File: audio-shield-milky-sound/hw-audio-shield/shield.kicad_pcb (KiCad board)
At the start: 2 copper layers, 53.3 x 53.8 mm, 30 parts, among them J1 JACK_TRS_6PINS, P1 CONN_12, P2 CONN_12, P3 CONN_01X02, SW2 SW_PUSH, U1 TLV320DAC3203, U2 LD39015M18R, U3 TPA2005D1

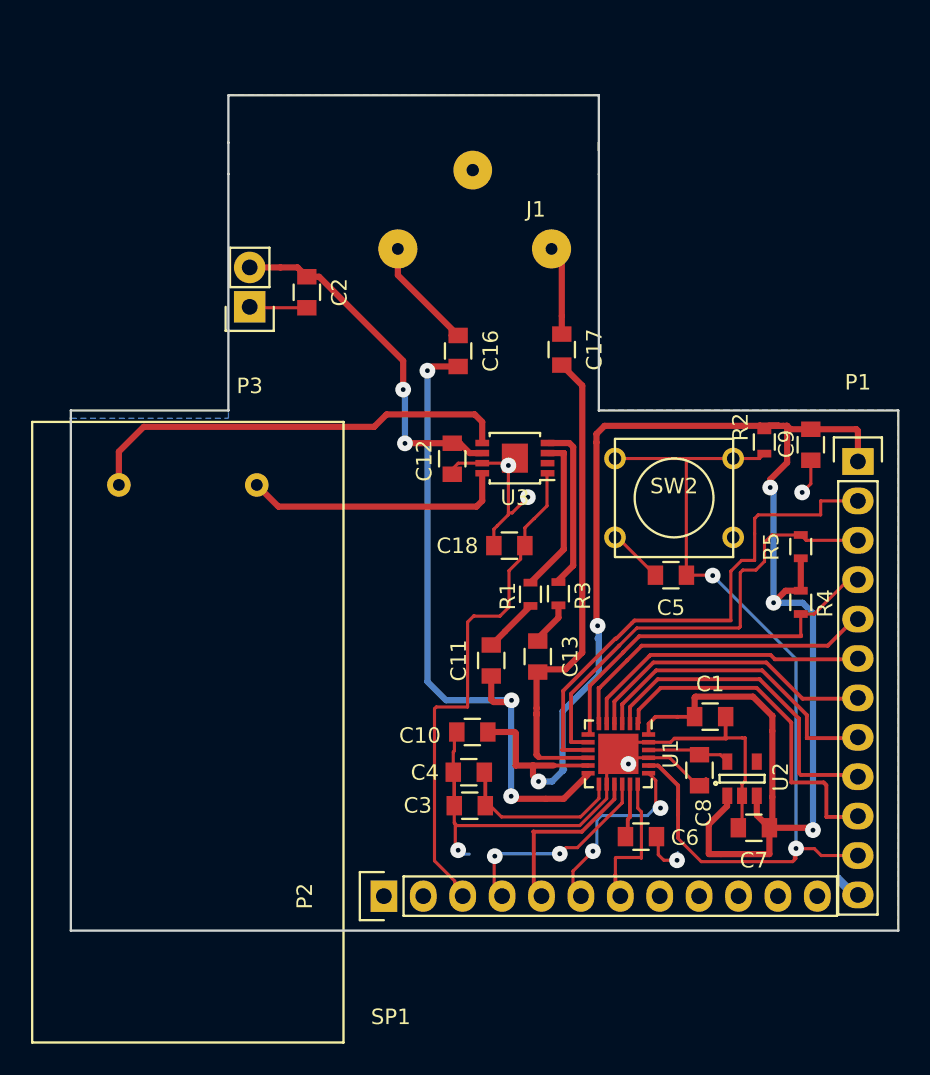
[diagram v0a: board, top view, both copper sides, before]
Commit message: Modification in the hdl sources and I2C Beep working
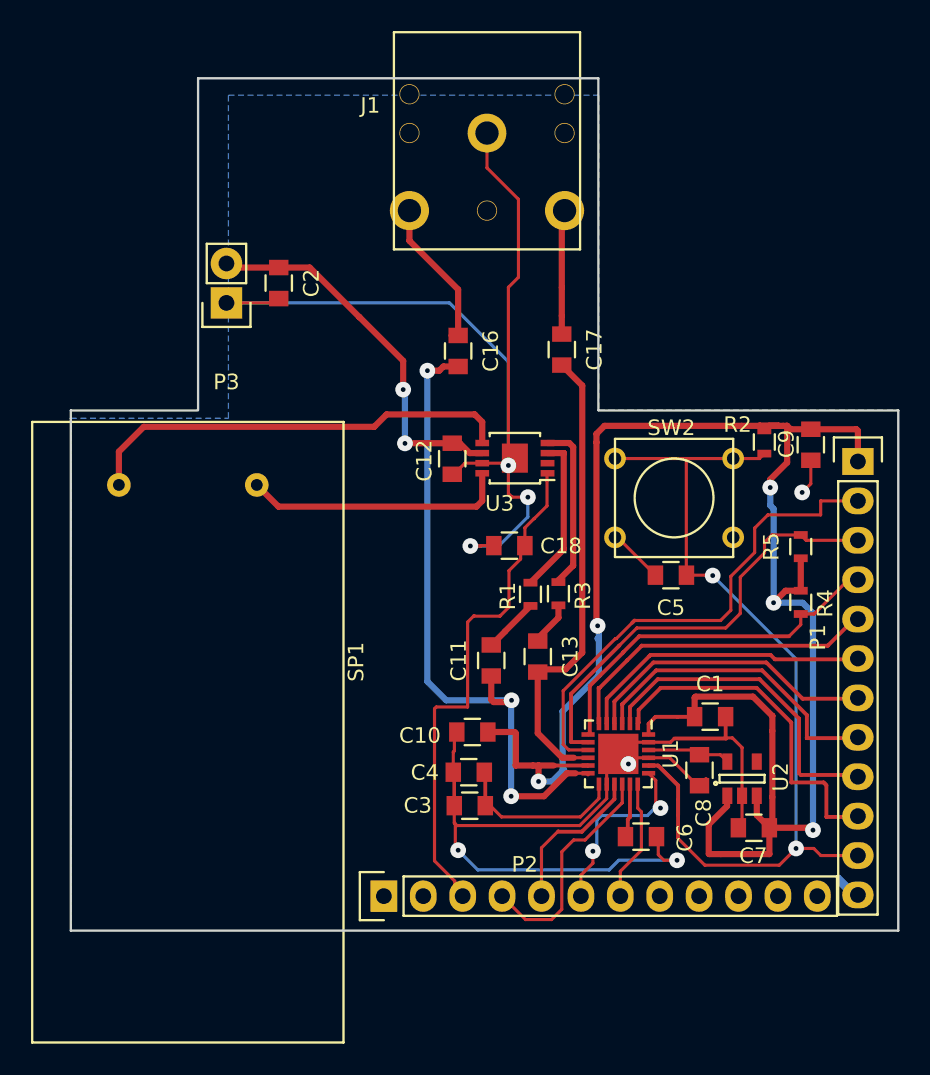
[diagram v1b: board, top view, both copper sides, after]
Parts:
- J1: footprint shield_foorprint:Jack Cliff FC68131 -> shield_foorprint:Jack.Cliff.FC68131
- moved J1 4.68 mm to (166.6, 46.2)
- moved C2 1.90 mm to (159.2, 62.4)
- moved P3 1.52 mm to (155.8, 63.7)
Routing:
- net GND: track 83.5 -> 149.0 mm, vias 6 -> 7
- net Net-(C17-Pad1): track 5.76 -> 8.03 mm
- net Net-(C16-Pad1): track 7.73 -> 9.89 mm
- net +5V: track 23.0 -> 25.0 mm
- net MISO: track 33.6 -> 32.0 mm
- net Net-(P2-Pad4): track 13.4 -> 14.9 mm, vias 2 -> 0
- net Haut-Parleur-R: track 32.0 -> 30.7 mm
- net Net-(P2-Pad5): track 11.6 -> 10.5 mm
- net SDA: track 30.4 -> 29.4 mm
- net /RESET: track 65.6 -> 64.7 mm
- net MCBIAS: track 9.10 -> 8.15 mm
- net SCL: track 24.7 -> 24.1 mm
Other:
- board size 53.3 x 53.8 mm -> 53.3 x 54.9 mm
- rule trace_min: 0.2 -> 0.1524
